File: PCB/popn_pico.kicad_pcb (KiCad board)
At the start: 2 copper layers, 180 x 100 mm, 4 parts

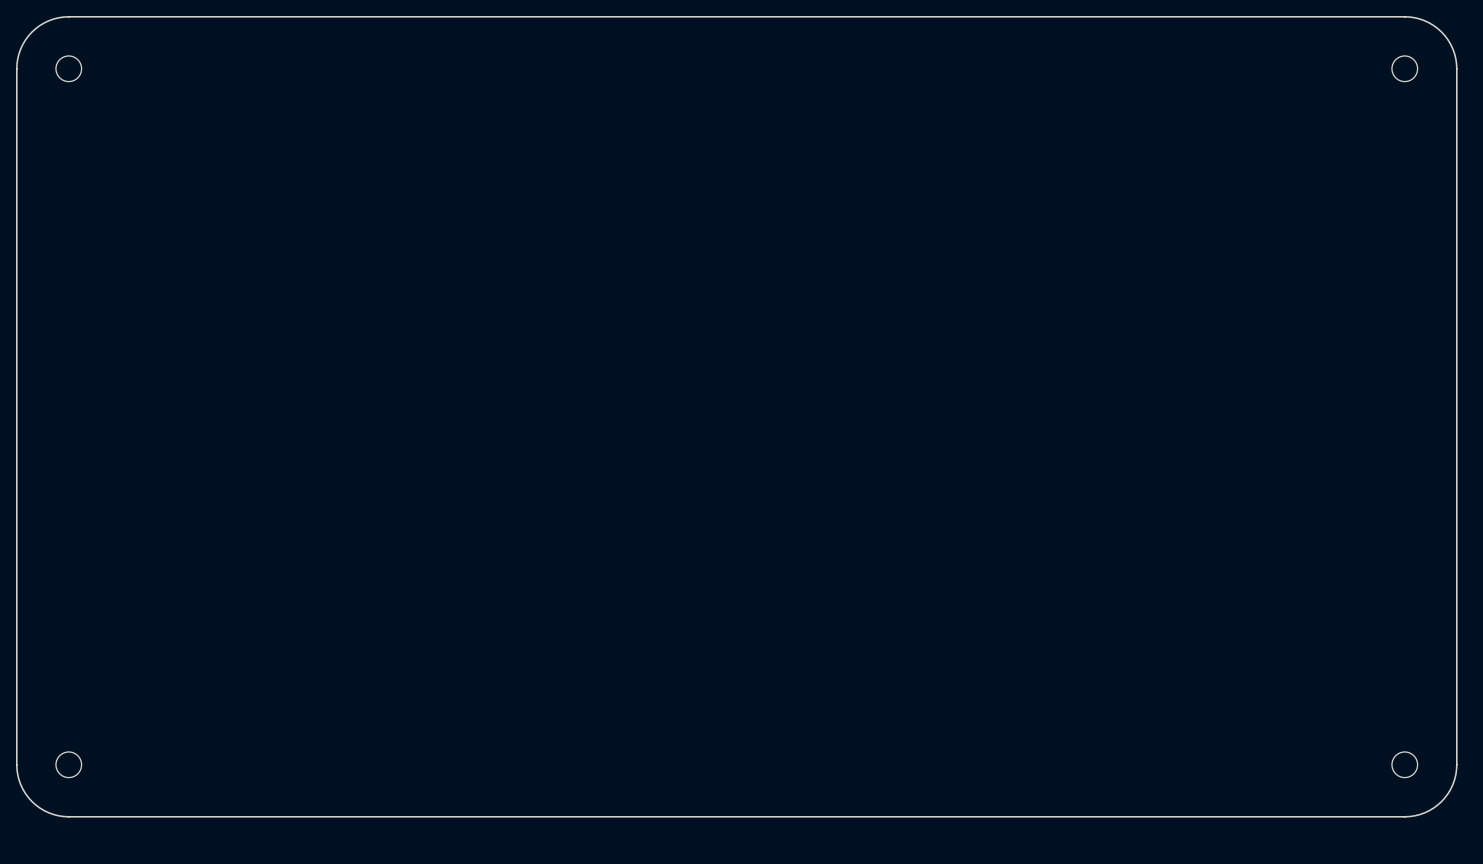
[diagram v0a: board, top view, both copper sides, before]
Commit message: Update PCB with libs and 3d models
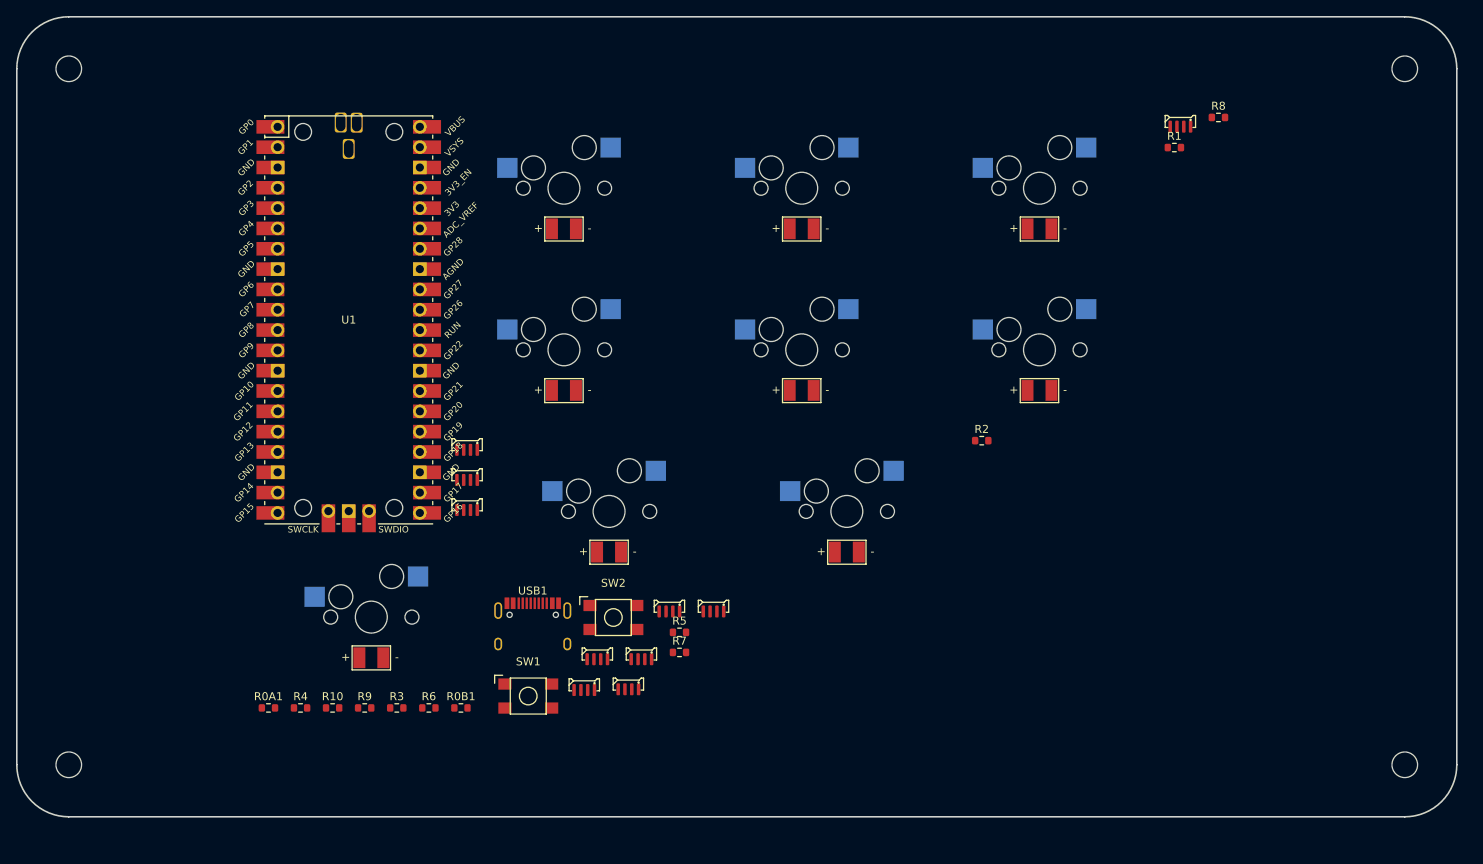
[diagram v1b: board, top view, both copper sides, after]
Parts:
- added LED1: WS2812B-4020, agg:WS2812B-4020, F.Cu at (127.0, 132.0)
- added LED10: WS2812B-4020, agg:WS2812B-4020, F.Cu at (137.6, 122.2)
- added LED2: WS2812B-4020, agg:WS2812B-4020, F.Cu at (134.1, 128.1)
- added LED3: WS2812B-4020, agg:WS2812B-4020, F.Cu at (112.3, 109.5)
- added LED4: WS2812B-4020, agg:WS2812B-4020, F.Cu at (201.5, 61.6)
- added LED5: WS2812B-4020, agg:WS2812B-4020, F.Cu at (132.5, 131.9)
- added LED6: WS2812B-4020, agg:WS2812B-4020, F.Cu at (143.2, 122.2)
- added LED7: WS2812B-4020, agg:WS2812B-4020, F.Cu at (128.6, 128.1)
- added LED8: WS2812B-4020, agg:WS2812B-4020, F.Cu at (112.3, 102.0)
- added LED9: WS2812B-4020, agg:WS2812B-4020, F.Cu at (112.3, 105.7)
- added MX1: MX-LED-B, MX_Only:MXOnly-1.5U-Hotswap-LED-SMD, F.Cu at (100.4, 123.5)
- added MX2: MX-LED, MX_Only:MXOnly-1.5U-Hotswap-LED-SMD, F.Cu at (124.5, 69.9)
- added MX3: MX-LED, MX_Only:MXOnly-1.5U-Hotswap-LED-SMD, F.Cu at (154.2, 69.9)
- added MX4: MX-LED, MX_Only:MXOnly-1.5U-Hotswap-LED-SMD, F.Cu at (124.5, 90.1)
- added MX5: MX-LED, MX_Only:MXOnly-1.5U-Hotswap-LED-SMD, F.Cu at (130.1, 110.3)
- added MX6: MX-LED-R, MX_Only:MXOnly-1.5U-Hotswap-LED-SMD, F.Cu at (154.2, 90.1)
- added MX7: MX-LED-R, MX_Only:MXOnly-1.5U-Hotswap-LED-SMD, F.Cu at (183.9, 69.9)
- added MX8: MX-LED-R, MX_Only:MXOnly-1.5U-Hotswap-LED-SMD, F.Cu at (159.8, 110.3)
- added MX9: MX-LED-R, MX_Only:MXOnly-1.5U-Hotswap-LED-SMD, F.Cu at (183.9, 90.1)
- added R0A1: 5K1, Resistor_SMD:R_0603_1608Metric, F.Cu at (87.5, 134.9)
- added R0B1: 5K1, Resistor_SMD:R_0603_1608Metric, F.Cu at (111.6, 134.9)
- added R1: 220R, Resistor_SMD:R_0603_1608Metric, F.Cu at (200.8, 64.8)
- added R10: 220R, Resistor_SMD:R_0603_1608Metric, F.Cu at (95.5, 134.9)
- added R2: 220R, Resistor_SMD:R_0603_1608Metric, F.Cu at (176.7, 101.5)
- added R3: 220R, Resistor_SMD:R_0603_1608Metric, F.Cu at (103.6, 134.9)
- added R4: 220R, Resistor_SMD:R_0603_1608Metric, F.Cu at (91.5, 134.9)
- added R5: 220R, Resistor_SMD:R_0603_1608Metric, F.Cu at (138.9, 125.4)
- added R6: 220R, Resistor_SMD:R_0603_1608Metric, F.Cu at (107.6, 134.9)
- added R7: 220R, Resistor_SMD:R_0603_1608Metric, F.Cu at (138.9, 127.9)
- added R8: 220R, Resistor_SMD:R_0603_1608Metric, F.Cu at (206.3, 61.1)
- added R9: 220R, Resistor_SMD:R_0603_1608Metric, F.Cu at (99.5, 134.9)
- added SW1: KAN4542-0701C, K2-1102SP-C4SC-04:KAN4542-0701C, F.Cu at (120.0, 133.4)
- added SW2: KAN4542-0701C, K2-1102SP-C4SC-04:KAN4542-0701C, F.Cu at (130.6, 123.6)
- added U1: Pico, MCU_RaspberryPi_and_Boards:RPi_Pico_SMD_TH, F.Cu at (97.6, 86.4)
- added USB1: U262-161N-4BVC11, Type-C:HRO-TYPE-C-31-M-12-Assembly, F.Cu at (120.6, 129.5)

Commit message: Finished layout
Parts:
- removed the REF** at (229.6, 55.0)
- removed the REF** at (62.6, 55.0)
- removed the REF** at (62.6, 142.0)
- added REF**: MountingHole_3.2mm_M3, MountingHole:MountingHole_3.2mm_M3, F.Cu at (232.3, 142.4)
- added REF**: MountingHole_3.2mm_M3, MountingHole:MountingHole_3.2mm_M3, F.Cu at (62.3, 142.4)
- added REF**: MountingHole_3.2mm_M3, MountingHole:MountingHole_3.2mm_M3, F.Cu at (207.3, 72.4)
- MX1: value MX-LED-B -> MX-BUTTON; footprint MX_Only:MXOnly-1.5U-Hotswap-LED-SMD -> MX_Only:MXOnly-Popn_Button-Hotswap-LED
- MX2, MX3, MX4, MX5: value MX-LED -> MX-BUTTON; footprint MX_Only:MXOnly-1.5U-Hotswap-LED-SMD -> MX_Only:MXOnly-Popn_Button-Hotswap-LED
- MX6, MX7, MX8, MX9: value MX-LED-R -> MX-BUTTON; footprint MX_Only:MXOnly-1.5U-Hotswap-LED-SMD -> MX_Only:MXOnly-Popn_Button-Hotswap-LED
- U1: footprint MCU_RaspberryPi_and_Boards:RPi_Pico_SMD_TH -> MCU_RaspberryPi_and_Boards:RPi_Pico_SMD; moved to B.Cu
- moved REF** 158.3 mm to (87.3, 72.4)
- moved R1 150.0 mm to (69.5, 137.4)
- moved LED4 144.2 mm to (67.3, 114.4), turned to -90 degrees
- moved R9 114.0 mm to (213.5, 137.4)
- moved LED9 103.0 mm to (215.3, 102.4)
- moved LED10 90.0 mm to (227.3, 114.4), turned to 90 degrees
- moved R2 89.4 mm to (87.3, 104.4)
- moved SW1 89.3 mm to (183.3, 70.4)
- moved SW2 83.7 mm to (195.3, 70.4)
- moved R10 76.8 mm to (157.1, 88.9)
- moved MX3 75.8 mm to (111.3, 132.4)
- moved LED8 75.6 mm to (187.3, 92.4)
- moved USB1 67.4 mm to (113.2, 62.5), turned to 180 degrees
- moved R20 66.7 mm to (114.5, 73.9), turned to -90 degrees
- moved MX7 62.5 mm to (183.3, 132.4)
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- renumbered R0A1 to R20, R0B1 to R21
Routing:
- net +5V: track 0.00 -> 398.0 mm
- net Net-(R1-Pad1): track 0.00 -> 109.8 mm, vias 0 -> 1
- net GND: track 0.00 -> 106.6 mm, vias 0 -> 12
- net Net-(MX1-Pad1): track 0.00 -> 100.8 mm
- net Net-(R3-Pad1): track 0.00 -> 92.3 mm, vias 0 -> 1
- net Net-(LED3-Pad3): track 0.00 -> 89.5 mm
- net Net-(MX3-Pad1): track 0.00 -> 83.2 mm
- net Net-(R7-Pad1): track 0.00 -> 75.9 mm, vias 0 -> 1
- net Net-(R5-Pad1): track 0.00 -> 74.1 mm, vias 0 -> 1
- net Net-(R2-Pad1): track 0.00 -> 71.9 mm, vias 0 -> 1
- net Net-(R9-Pad1): track 0.00 -> 71.7 mm, vias 0 -> 1
- net Net-(SW2-Pad1): track 0.00 -> 70.4 mm
- net Net-(MX7-Pad1): track 0.00 -> 68.4 mm
- net Net-(MX5-Pad1): track 0.00 -> 66.5 mm
- net Net-(MX2-Pad1): track 0.00 -> 63.0 mm
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- added copper zone on B.Cu, net GND
- added copper zone on F.Cu, net GND
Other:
- board size 180 x 100 mm -> 180 x 85 mm
